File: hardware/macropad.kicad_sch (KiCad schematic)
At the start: 27 parts, among them J2 Conn_01x06, J3 I2C Screen, J4 SPI Screen, SW1 SW_Push, SW10 SW_Push, SW2 SW_Push, SW3 SW_Push, SW4 SW_Push, SW5 SW_Push, SW6 SW_Push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

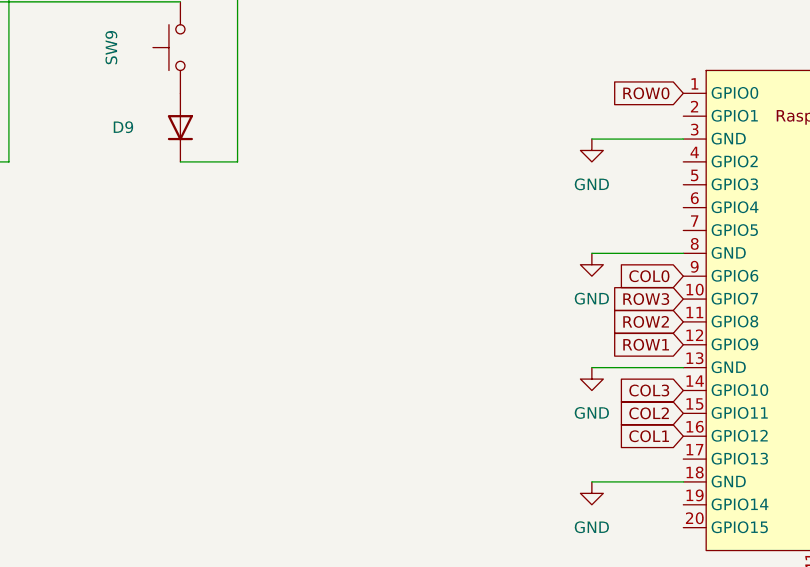
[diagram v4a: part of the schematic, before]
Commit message: :construction: Edit pi pico to remove tht pads & add castellated pads for D+/D-
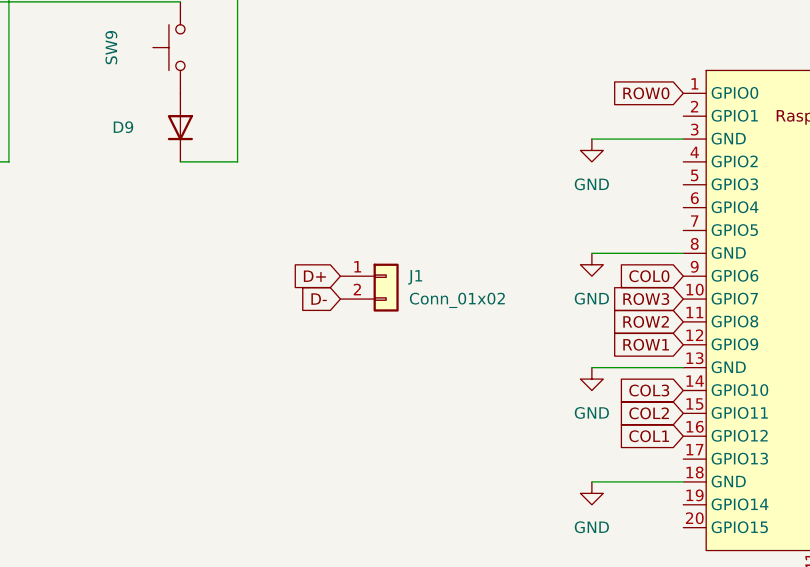
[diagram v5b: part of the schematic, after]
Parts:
- added J1: Conn_01x02, Connector_PinHeader_2.00mm:PinHeader_1x02_P2.00mm_Vertical, symbol Connector_Generic:Conn_01x02
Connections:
- new net D+: J1.1 (Pin_1)
- new net D-: J1.2 (Pin_2)
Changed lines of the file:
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@@
+    )
+  )
+  (global_label "D+" (shape input) (at 148.59 120.65 180) (fields_autoplaced)
+    (effects (font (size 1.27 1.27)) (justify right))
+    (property "Références Inter-Feuilles" "${INTERSHEET_REFS}" (id 0) (at 143.3345 120.5706 0)
+      (effects (font (size 1.27 1.27)) (justify right) hide)
     )
   )
@@
     (property "Intersheet References" "${INTERSHEET_REFS}" (id 0) (at 232.1017 138.3506 0)
       (effects (font (size 1.27 1.27)) (justify left) hide)
+    )
+  )
+  (global_label "D-" (shape input) (at 148.59 123.19 180) (fields_autoplaced)
+    (effects (font (size 1.27 1.27)) (justify right))
+    (property "Références Inter-Feuilles" "${INTERSHEET_REFS}" (id 0) (at 143.3345 123.1106 0)
+      (effects (font (size 1.27 1.27)) (justify right) hide)
     )
   )
@@
     )
     (pin "1")
+  )
+  (symbol (lib_id "Connector_Generic:Conn_01x02") (at 153.67 120.65 0) (unit 1)
+    (in_bom yes) (on_board yes) (fields_autoplaced)
+    (property "Reference" "J1" (id 0) (at 156.21 120.6499 0)
+      (effects (font (size 1.27 1.27)) (justify left))
+    )
+    (property "Value" "Conn_01x02" (id 1) (at 156.21 123.1899 0)
+      (effects (font (size 1.27 1.27)) (justify left))
+    )
+    (property "Footprint" "Connector_PinHeader_2.00mm:PinHeader_1x02_P2.00mm_Vertical" (id 2) (at 153.67 120.65 0)
+      (effects (font (size 1.27 1.27)) hide)
+    )
+    (property "Datasheet" "~" (id 3) (at 153.67 120.65 0)
+      (effects (font (size 1.27 1.27)) hide)
+    )
+    (pin "1")
+    (pin "2")
   )
   (symbol (lib_id "Switch:SW_Push") (at 170.18 22.86 0) (mirror x) (unit 1)
@@
       (reference "H4") (unit 1) (value "MountingHole") (footprint "MountingHole:MountingHole_3.2mm_M3")
     )
+    (path "/b101a5d3-e6be-489b-b38d-e6a56dc3ad0f"
+      (reference "J1") (unit 1) (value "Conn_01x02") (footprint "Connector_PinHeader_2.00mm:PinHeader_1x02_P2.00mm_Vertical")
+    )
     (path "/edaf29ef-f159-451d-a7e6-d95b592ffd95"

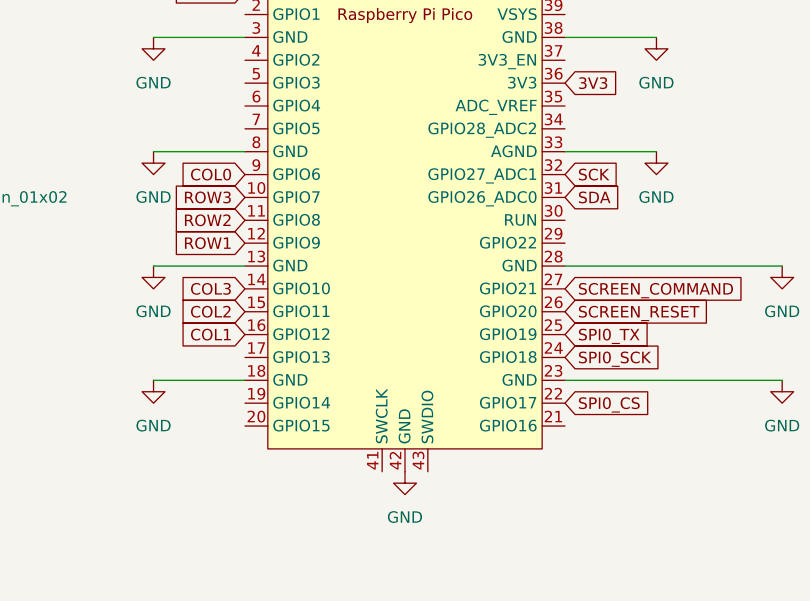
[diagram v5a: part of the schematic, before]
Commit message: :truck: Move screen headers, before changing footprint
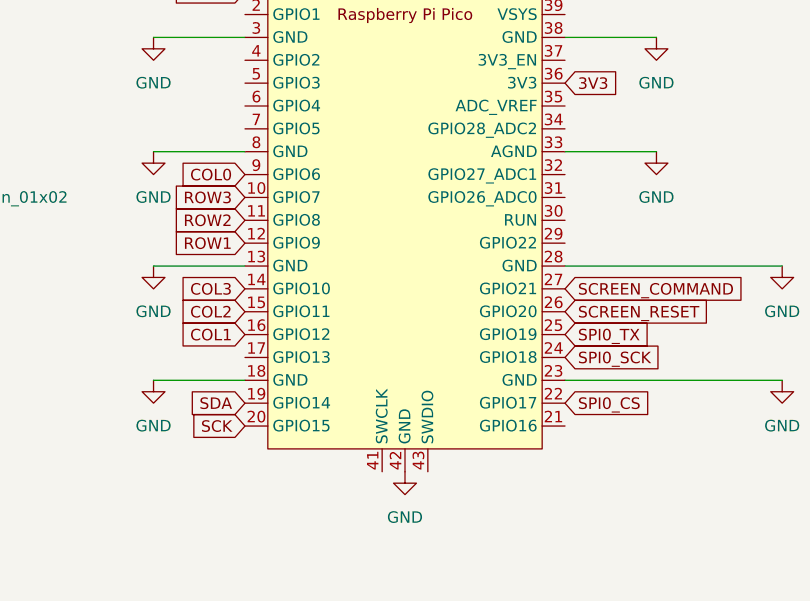
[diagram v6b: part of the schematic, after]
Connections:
- net SCK: now also U1.20 (GPIO15); no longer U1.32 (GPIO27_ADC1)
- net SDA: now also U1.19 (GPIO14); no longer U1.31 (GPIO26_ADC0)
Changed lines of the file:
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@@
     )
   )
-  (global_label "SDA" (shape input) (at 222.25 123.19 0) (fields_autoplaced)
-    (effects (font (size 1.27 1.27)) (justify left))
-    (property "Intersheet References" "${INTERSHEET_REFS}" (id 0) (at 228.2312 123.1106 0)
-      (effects (font (size 1.27 1.27)) (justify left) hide)
+  (global_label "SDA" (shape input) (at 186.69 146.05 180) (fields_autoplaced)
+    (effects (font (size 1.27 1.27)) (justify right))
+    (property "Intersheet References" "${INTERSHEET_REFS}" (id 0) (at 180.7088 146.1294 0)
+      (effects (font (size 1.27 1.27)) (justify right) hide)
     )
   )
@@
     )
   )
-  (global_label "SCK" (shape input) (at 222.25 120.65 0) (fields_autoplaced)
-    (effects (font (size 1.27 1.27)) (justify left))
-    (property "Intersheet References" "${INTERSHEET_REFS}" (id 0) (at 228.4126 120.5706 0)
-      (effects (font (size 1.27 1.27)) (justify left) hide)
+  (global_label "SCK" (shape input) (at 186.69 148.59 180) (fields_autoplaced)
+    (effects (font (size 1.27 1.27)) (justify right))
+    (property "Intersheet References" "${INTERSHEET_REFS}" (id 0) (at 180.5274 148.6694 0)
+      (effects (font (size 1.27 1.27)) (justify right) hide)
     )
   )

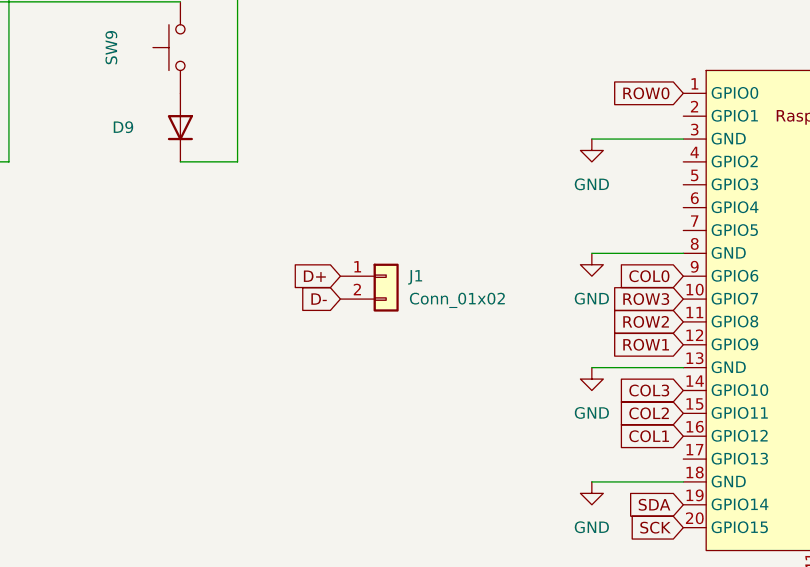
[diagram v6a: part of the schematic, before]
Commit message: :construction: Change OLED footprint, reroute to accomodate. Delete USB pads, leave hole instead
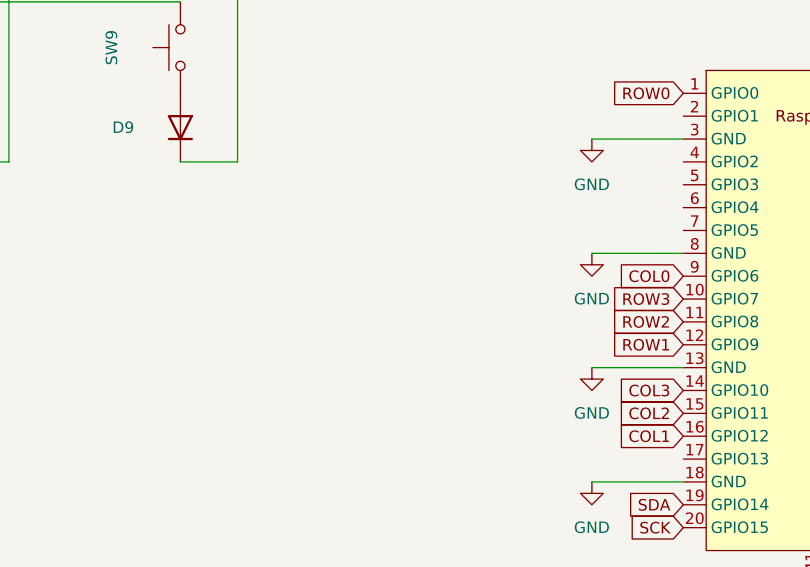
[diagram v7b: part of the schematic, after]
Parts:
- removed J1: Conn_01x02, Connector_PinHeader_2.00mm:PinHeader_1x02_P2.00mm_Vertical, symbol Connector_Generic:Conn_01x02
- J3: footprint Connector_PinHeader_2.54mm:PinHeader_1x04_P2.54mm_Vertical -> nn_lib:I2C_1.3inch_OLED
- J4: footprint Connector_PinHeader_2.54mm:PinHeader_1x07_P2.54mm_Vertical -> nn_lib:SPI_1.3inch_OLED
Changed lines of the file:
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@@
-    )
-  )
-  (global_label "D+" (shape input) (at 148.59 120.65 180) (fields_autoplaced)
-    (effects (font (size 1.27 1.27)) (justify right))
-    (property "Références Inter-Feuilles" "${INTERSHEET_REFS}" (id 0) (at 143.3345 120.5706 0)
-      (effects (font (size 1.27 1.27)) (justify right) hide)
     )
   )
@@
     )
   )
-  (global_label "D-" (shape input) (at 148.59 123.19 180) (fields_autoplaced)
-    (effects (font (size 1.27 1.27)) (justify right))
-    (property "Références Inter-Feuilles" "${INTERSHEET_REFS}" (id 0) (at 143.3345 123.1106 0)
-      (effects (font (size 1.27 1.27)) (justify right) hide)
-    )
-  )
   (global_label "ROW2" (shape input) (at 186.69 125.73 180) (fields_autoplaced)
     (effects (font (size 1.27 1.27)) (justify right))
@@
       (effects (font (size 1.27 1.27)) (justify left))
     )
-    (property "Footprint" "Connector_PinHeader_2.54mm:PinHeader_1x07_P2.54mm_Vertical" (id 2) (at 209.55 74.93 0)
+    (property "Footprint" "nn_lib:SPI_1.3inch_OLED" (id 2) (at 209.55 74.93 0)
       (effects (font (size 1.27 1.27)) hide)
     )
@@
       (effects (font (size 1.27 1.27)) (justify left))
     )
-    (property "Footprint" "Connector_PinHeader_2.54mm:PinHeader_1x04_P2.54mm_Vertical" (id 2) (at 209.55 58.42 0)
+    (property "Footprint" "nn_lib:I2C_1.3inch_OLED" (id 2) (at 209.55 58.42 0)
       (effects (font (size 1.27 1.27)) hide)
     )
@@
     )
     (pin "1")
-  )
-  (symbol (lib_id "Connector_Generic:Conn_01x02") (at 153.67 120.65 0) (unit 1)
-    (in_bom yes) (on_board yes) (fields_autoplaced)
-    (property "Reference" "J1" (id 0) (at 156.21 120.6499 0)
-      (effects (font (size 1.27 1.27)) (justify left))
-    )
-    (property "Value" "Conn_01x02" (id 1) (at 156.21 123.1899 0)
-      (effects (font (size 1.27 1.27)) (justify left))
-    )
-    (property "Footprint" "Connector_PinHeader_2.00mm:PinHeader_1x02_P2.00mm_Vertical" (id 2) (at 153.67 120.65 0)
-      (effects (font (size 1.27 1.27)) hide)
-    )
-    (property "Datasheet" "~" (id 3) (at 153.67 120.65 0)
-      (effects (font (size 1.27 1.27)) hide)
-    )
-    (pin "1")
-    (pin "2")
   )
   (symbol (lib_id "Switch:SW_Push") (at 170.18 22.86 0) (mirror x) (unit 1)
@@
       (reference "H4") (unit 1) (value "MountingHole") (footprint "MountingHole:MountingHole_3.2mm_M3")
     )
-    (path "/b101a5d3-e6be-489b-b38d-e6a56dc3ad0f"
-      (reference "J1") (unit 1) (value "Conn_01x02") (footprint "Connector_PinHeader_2.00mm:PinHeader_1x02_P2.00mm_Vertical")
-    )
     (path "/edaf29ef-f159-451d-a7e6-d95b592ffd95"
       (reference "J2") (unit 1) (value "Conn_01x06") (footprint "Connector_PinHeader_2.54mm:PinHeader_1x06_P2.54mm_Vertical")
     )
     (path "/8ee542c5-c2bc-43b0-ad1a-50bd2362b045"
-      (reference "J3") (unit 1) (value "I2C Screen") (footprint "Connector_PinHeader_2.54mm:PinHeader_1x04_P2.54mm_Vertical")
+      (reference "J3") (unit 1) (value "I2C Screen") (footprint "nn_lib:I2C_1.3inch_OLED")
     )
     (path "/5c3a4c73-114c-4037-b6c5-a451d426c74f"
-      (reference "J4") (unit 1) (value "SPI Screen") (footprint "Connector_PinHeader_2.54mm:PinHeader_1x07_P2.54mm_Vertical")
+      (reference "J4") (unit 1) (value "SPI Screen") (footprint "nn_lib:SPI_1.3inch_OLED")
     )
     (path "/ea347c49-517e-4a6a-a6e9-f2bd7f3d4eac"
